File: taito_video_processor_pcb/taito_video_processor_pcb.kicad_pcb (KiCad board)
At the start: 2 copper layers, 304.8 x 279.4 mm, 112 parts, among them U1 245_1, U10 4116, U100 LS00, U101 LS08, U102 LS10, U103 LS00, U104 157_1, U105 299_1, U106 299_1, U107 299_1, U108 299_1, U109 299_1, U11 4116, U110 299_1, U12 4116, U13 4116, U14 4116, U15 4116, U16 4116, U17 4116, U18 68A45, U19 86_2, U2 245_1, U20 86_1, U21 157_1, U22 LS32, U23 161_1, U24 LS04, U25 374_1, U26 4116, U27 4116, U28 4116, U29 4116, U3 2114, U30 4116, U31 4116, U32 4116, U33 4116, U34 LS374, U35 153_1, U36 LS74, U37 LS08, U38 74S113, U39 LS04, U4 2114, U40 7417, U41 4116, U42 4116, U43 4116, U44 4116, U45 4116, U46 4116, U47 4116, U48 4116, U49 LS32, U5 157_1, U50 86_3, U51 LS86, U52 153_1, U53 153_1, U54 153_1, U55 157_1, U56 2148_1, U57 2148_2, U58 7417, U59 4116, U6 157_1, U60 4116, U61 4116, U62 4116, U63 4116, U64 4116, U65 4116, U66 4116, U67 LS32, U68 244_2, U69 245_1, U7 LS74, U70 374_1, U71 374_1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

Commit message: Continued layout
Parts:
- added J3: 50pin, taito_video_processor_pcb:50Pin, F.Cu at (208.3, 342.9)
- added J6: 50pin, taito_video_processor_pcb:50Pin, F.Cu at (208.3, 90.2)
- added REF**: hole_15, taito_video_processor_pcb:hole_15, F.Cu at (355.6, 83.8)
- added REF**: hole_15, taito_video_processor_pcb:hole_15, F.Cu at (449.6, 83.8)
- added REF**: hole_15, taito_video_processor_pcb:hole_15, F.Cu at (161.3, 84.5)
- added REF**: hole_15, taito_video_processor_pcb:hole_15, F.Cu at (160.0, 348.0)
- moved REF** 0.63 mm to (449.6, 348.0)
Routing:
- added copper zone on B.Cu, net GND

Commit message: Placed components
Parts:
- added C1: .1uf, taito_video_processor_pcb:GenericComp, F.Cu at (299.7, 86.4)
- added C10: .1uf, taito_video_processor_pcb:GenericComp, F.Cu at (176.5, 104.1)
- added C11: .1uf, taito_video_processor_pcb:GenericComp, F.Cu at (196.8, 123.8)
- added C12: .1uf, taito_video_processor_pcb:GenericComp, F.Cu at (207.6, 115.6)
- added C13: .1uf, taito_video_processor_pcb:GenericComp, F.Cu at (255.3, 101.6)
- added C14: 100pf, taito_video_processor_pcb:GenericComp, F.Cu at (269.2, 108.0)
- added C15: .1uf, taito_video_processor_pcb:GenericComp, F.Cu at (284.5, 109.2)
- added C16: .1uf, taito_video_processor_pcb:GenericComp, F.Cu at (316.2, 111.8)
- added C17: .1uf, taito_video_processor_pcb:GenericComp, F.Cu at (331.5, 111.8)
- added C18: .1uf, taito_video_processor_pcb:GenericComp, F.Cu at (346.7, 111.8)
- added C19: .1uf, taito_video_processor_pcb:GenericComp, F.Cu at (361.9, 111.8)
- added C2: .1uf, taito_video_processor_pcb:GenericComp, F.Cu at (303.5, 90.2)
- added C20: .1uf, taito_video_processor_pcb:GenericComp, F.Cu at (377.2, 111.8)
- added C21: .1uf, taito_video_processor_pcb:GenericComp, F.Cu at (392.4, 111.8)
- added C22: 10uf, taito_video_processor_pcb:CapA, F.Cu at (406.4, 101.6)
- added C23: .1uf, taito_video_processor_pcb:GenericComp, F.Cu at (420.4, 97.8)
- added C24: .1uf, taito_video_processor_pcb:GenericComp, F.Cu at (448.3, 99.1)
- added C25: .1uf, taito_video_processor_pcb:GenericComp, F.Cu at (448.3, 104.1)
- added C26: .1uf, taito_video_processor_pcb:GenericComp, F.Cu at (161.3, 138.4)
- added C27: .1uf, taito_video_processor_pcb:GenericComp, F.Cu at (189.2, 139.7)
- added C28: .1uf, taito_video_processor_pcb:GenericComp, F.Cu at (207.0, 143.5)
- added C29: .1uf, taito_video_processor_pcb:GenericComp, F.Cu at (224.8, 146.1)
- added C3: .1uf, taito_video_processor_pcb:GenericComp, F.Cu at (318.8, 90.2)
- added C30: .1uf, taito_video_processor_pcb:GenericComp, F.Cu at (237.5, 148.6)
- added C31: 100pf, taito_video_processor_pcb:GenericComp, F.Cu at (271.8, 123.2)
- added C32: .1uf, taito_video_processor_pcb:GenericComp, F.Cu at (285.8, 151.1)
- added C33: .1uf, taito_video_processor_pcb:GenericComp, F.Cu at (312.4, 127.6)
- added C34: .1uf, taito_video_processor_pcb:GenericComp, F.Cu at (329.6, 127.6)
- added C35: .1uf, taito_video_processor_pcb:GenericComp, F.Cu at (316.2, 146.1)
- added C36: .1uf, taito_video_processor_pcb:GenericComp, F.Cu at (331.5, 146.1)
- added C37: .1uf, taito_video_processor_pcb:GenericComp, F.Cu at (346.7, 146.1)
- added C38: .1uf, taito_video_processor_pcb:GenericComp, F.Cu at (360.7, 134.6)
- added C39: .1uf, taito_video_processor_pcb:GenericComp, F.Cu at (361.9, 146.1)
- added C4: .1uf, taito_video_processor_pcb:GenericComp, F.Cu at (334.0, 90.2)
- added C40: .1uf, taito_video_processor_pcb:GenericComp, F.Cu at (375.9, 134.6)
- added C41: .1uf, taito_video_processor_pcb:GenericComp, F.Cu at (377.2, 146.1)
- added C42: 10uf, taito_video_processor_pcb:CapA, F.Cu at (391.8, 135.9)
- added C43: .1uf, taito_video_processor_pcb:GenericComp, F.Cu at (398.8, 127.6)
- added C44: 10uf, taito_video_processor_pcb:CapA, F.Cu at (407.7, 128.9)
- added C45: 10uf, taito_video_processor_pcb:CapA, F.Cu at (417.8, 127.0)
- added C46: .1uf, taito_video_processor_pcb:GenericComp, F.Cu at (448.3, 129.5)
- added C47: .1uf, taito_video_processor_pcb:GenericComp, F.Cu at (448.3, 134.6)
- added C48: .1uf, taito_video_processor_pcb:GenericComp, F.Cu at (448.3, 139.7)
- added C49: .1uf, taito_video_processor_pcb:GenericComp, F.Cu at (448.3, 151.1)
- added C5: .1uf, taito_video_processor_pcb:GenericComp, F.Cu at (349.2, 90.2)
- added C50: .1uf, taito_video_processor_pcb:GenericComp, F.Cu at (222.2, 181.6)
- added C51: .1uf, taito_video_processor_pcb:GenericComp, F.Cu at (255.3, 174.0)
- added C52: .1uf, taito_video_processor_pcb:GenericComp, F.Cu at (270.5, 174.0)
- added C53: .1uf, taito_video_processor_pcb:GenericComp, F.Cu at (307.3, 163.8)
- added C54: .1uf, taito_video_processor_pcb:GenericComp, F.Cu at (321.3, 162.6)
- added C55: .1uf, taito_video_processor_pcb:GenericComp, F.Cu at (314.3, 181.6)
- added C56: .1uf, taito_video_processor_pcb:GenericComp, F.Cu at (331.5, 181.6)
- added C57: .1uf, taito_video_processor_pcb:GenericComp, F.Cu at (336.6, 163.2)
- added C58: .1uf, taito_video_processor_pcb:GenericComp, F.Cu at (351.8, 163.2)
- added C59: .1uf, taito_video_processor_pcb:GenericComp, F.Cu at (361.9, 181.6)
- added C6: .1uf, taito_video_processor_pcb:GenericComp, F.Cu at (364.5, 90.2)
- added C60: .1uf, taito_video_processor_pcb:GenericComp, F.Cu at (377.2, 181.6)
- added C61: 10uf, taito_video_processor_pcb:CapA, F.Cu at (391.8, 171.4)
- added C62: .1uf, taito_video_processor_pcb:GenericComp, F.Cu at (398.8, 163.8)
- added C63: 10uf, taito_video_processor_pcb:CapA, F.Cu at (407.0, 167.6)
- added C64: .1uf, taito_video_processor_pcb:GenericComp, F.Cu at (414.0, 162.6)
- added C65: 470pf, taito_video_processor_pcb:GenericComp, F.Cu at (448.3, 162.6)
- added C66: .1uf, taito_video_processor_pcb:GenericComp, F.Cu at (448.3, 168.9)
- added C67: .1uf, taito_video_processor_pcb:GenericComp, F.Cu at (161.3, 199.4)
- added C68: .1uf, taito_video_processor_pcb:GenericComp, F.Cu at (207.6, 209.6)
- added C69: .1uf, taito_video_processor_pcb:GenericComp, F.Cu at (239.4, 209.6)
- added C7: .1uf, taito_video_processor_pcb:GenericComp, F.Cu at (379.7, 90.2)
- added C70: .1uf, taito_video_processor_pcb:GenericComp, F.Cu at (253.4, 209.6)
- added C71: .1uf, taito_video_processor_pcb:GenericComp, F.Cu at (269.2, 209.6)
- added C72: .1uf, taito_video_processor_pcb:GenericComp, F.Cu at (316.2, 217.2)
- added C73: .1uf, taito_video_processor_pcb:GenericComp, F.Cu at (322.6, 199.4)
- added C74: .1uf, taito_video_processor_pcb:GenericComp, F.Cu at (337.8, 199.4)
- added C75: .1uf, taito_video_processor_pcb:GenericComp, F.Cu at (346.7, 217.2)
- added C76: .1uf, taito_video_processor_pcb:GenericComp, F.Cu at (377.2, 217.2)
- added C77: 10uf, taito_video_processor_pcb:CapA, F.Cu at (391.8, 207.0)
- added C78: .1uf, taito_video_processor_pcb:GenericComp, F.Cu at (398.8, 199.4)
- added C79: .1uf, taito_video_processor_pcb:GenericComp, F.Cu at (406.4, 217.2)
- added C8: .1uf, taito_video_processor_pcb:GenericComp, F.Cu at (395.0, 90.2)
- added C80: 10uf, taito_video_processor_pcb:CapA, F.Cu at (408.3, 197.5)
- added C81: .1uf, taito_video_processor_pcb:GenericComp, F.Cu at (413.4, 191.1)
- added C82: .1uf, taito_video_processor_pcb:GenericComp, F.Cu at (448.3, 204.5)
- added C87: .1uf, taito_video_processor_pcb:GenericComp, F.Cu at (440.1, 226.1)
- added C9: 10uf, taito_video_processor_pcb:CapA, F.Cu at (408.3, 88.9)
- added FB1: Ferrite_Bead, taito_video_processor_pcb:FB, F.Cu at (422.9, 109.2)
- added FB2: Ferrite_Bead, taito_video_processor_pcb:FB, F.Cu at (428.0, 109.2)
- added FB3: Ferrite_Bead, taito_video_processor_pcb:FB, F.Cu at (422.9, 123.8)
- added FB4: Ferrite_Bead, taito_video_processor_pcb:FB, F.Cu at (422.9, 141.0)
- added FB5: Ferrite_Bead, taito_video_processor_pcb:FB, F.Cu at (428.0, 141.0)
- added FB6: Ferrite_Bead, taito_video_processor_pcb:FB, F.Cu at (422.9, 157.5)
- added FB7: Ferrite_Bead, taito_video_processor_pcb:FB, F.Cu at (428.0, 157.5)
- added J1: 14pin, taito_video_processor_pcb:con_14pin, F.Cu at (434.3, 306.4)
- added J19: 2pin, taito_video_processor_pcb:con_2pin, F.Cu at (434.3, 160.0)
- added J2: 14pin, taito_video_processor_pcb:con_14pin, F.Cu at (434.3, 123.5)
- added Q1: 2N3904, taito_video_processor_pcb:Trans, F.Cu at (279.4, 198.1)
- added Q2: 2N3904, taito_video_processor_pcb:Trans, F.Cu at (287.0, 198.1)
- added Q3: 2N3904, taito_video_processor_pcb:Trans, F.Cu at (287.0, 190.5)
- added Q4: 2N3904, taito_video_processor_pcb:Trans, F.Cu at (297.2, 190.5)
- added Q5: 2N3904, taito_video_processor_pcb:Trans, F.Cu at (297.2, 198.1)
- added Q6: 2N3904, taito_video_processor_pcb:Trans, F.Cu at (299.7, 207.0)
- added Q7: 2N3904, taito_video_processor_pcb:Trans, F.Cu at (299.7, 217.2)
- added Q8: 2N3905, taito_video_processor_pcb:Trans, F.Cu at (254.0, 341.6)
- added R1: 33, taito_video_processor_pcb:GenericComp, F.Cu at (420.4, 90.2)
- added R10: 33, taito_video_processor_pcb:GenericComp, F.Cu at (406.4, 143.5)
- added R11: ?, taito_video_processor_pcb:GenericComp, F.Cu at (252.7, 188.0)
- added R12: ?, taito_video_processor_pcb:GenericComp, F.Cu at (268.0, 185.4)
- added R13: 82, taito_video_processor_pcb:GenericComp, F.Cu at (283.2, 179.1)
- added R14: 180, taito_video_processor_pcb:GenericComp, F.Cu at (285.8, 179.1)
- added R15: 270, taito_video_processor_pcb:GenericComp, F.Cu at (283.2, 166.4)
- added R16: 150, taito_video_processor_pcb:GenericComp, F.Cu at (285.8, 166.4)
- added R17: 150, taito_video_processor_pcb:GenericComp, F.Cu at (298.4, 166.4)
- added R18: 270, taito_video_processor_pcb:GenericComp, F.Cu at (301.0, 166.4)
- added R19: 180, taito_video_processor_pcb:GenericComp, F.Cu at (298.4, 179.1)
- added R2: 1.5k, taito_video_processor_pcb:GenericComp, F.Cu at (274.3, 123.2)
- added R20: 82, taito_video_processor_pcb:GenericComp, F.Cu at (301.0, 179.1)
- added R21: 33, taito_video_processor_pcb:GenericComp, F.Cu at (422.9, 180.3)
- added R22: ?, taito_video_processor_pcb:GenericComp, F.Cu at (203.2, 199.4)
- added R23: ?, taito_video_processor_pcb:GenericComp, F.Cu at (208.3, 195.6)
- added R24: ?, taito_video_processor_pcb:GenericComp, F.Cu at (218.4, 191.8)
- added R25: ?, taito_video_processor_pcb:GenericComp, F.Cu at (223.5, 205.7)
- added R26: ?, taito_video_processor_pcb:GenericComp, F.Cu at (269.2, 196.8)
- added R27: ?, taito_video_processor_pcb:GenericComp, F.Cu at (269.2, 199.4)
- added R28: 180, taito_video_processor_pcb:GenericComp, F.Cu at (283.2, 195.6)
- added R29: 470, taito_video_processor_pcb:GenericComp, F.Cu at (290.8, 195.6)
- added R3: 270, taito_video_processor_pcb:GenericComp, F.Cu at (284.5, 119.4)
- added R30: 470, taito_video_processor_pcb:GenericComp, F.Cu at (293.4, 195.6)
- added R31: 470, taito_video_processor_pcb:GenericComp, F.Cu at (301.0, 195.6)
- added R32: 470, taito_video_processor_pcb:GenericComp, F.Cu at (303.5, 195.6)
- added R33: 470, taito_video_processor_pcb:GenericComp, F.Cu at (306.1, 195.6)
- added R34: 680, taito_video_processor_pcb:GenericComp, F.Cu at (283.2, 209.6)
- added R35: 390, taito_video_processor_pcb:GenericComp, F.Cu at (285.8, 209.6)
- added R36: 33, taito_video_processor_pcb:GenericComp, F.Cu at (422.9, 212.1)
- added R39: 330, taito_video_processor_pcb:GenericComp, F.Cu at (225.4, 231.1)
- added R4: 270, taito_video_processor_pcb:GenericComp, F.Cu at (284.5, 121.9)
- added R40: 330, taito_video_processor_pcb:GenericComp, F.Cu at (230.5, 231.1)
- added R41: 330, taito_video_processor_pcb:GenericComp, F.Cu at (233.0, 231.1)
- added R42: 330, taito_video_processor_pcb:GenericComp, F.Cu at (235.6, 231.1)
- added R43: 330, taito_video_processor_pcb:GenericComp, F.Cu at (238.1, 231.1)
- added R44: 330, taito_video_processor_pcb:GenericComp, F.Cu at (240.7, 231.1)
- added R5: 270, taito_video_processor_pcb:GenericComp, F.Cu at (284.5, 124.5)
- added R6: 3.3k, taito_video_processor_pcb:GenericComp, F.Cu at (255.3, 138.4)
- added R7: 220, taito_video_processor_pcb:GenericComp, F.Cu at (268.0, 141.0)
- added R8: 2.2k, taito_video_processor_pcb:GenericComp, F.Cu at (270.5, 141.0)
- added R9: ?, taito_video_processor_pcb:GenericComp, F.Cu at (299.7, 130.8)
- added RP1: 1K, taito_video_processor_pcb:RP, F.Cu at (299.7, 108.0)
- added RP2: 47K, taito_video_processor_pcb:RP, F.Cu at (161.9, 299.7)
- added RP3: 3.3k, taito_video_processor_pcb:RP, F.Cu at (193.7, 287.0)
- added RP4: 3.3k, taito_video_processor_pcb:RP, F.Cu at (193.7, 322.6)
- added RP5: 3.3k, taito_video_processor_pcb:RP, F.Cu at (234.9, 334.0)
- added TP1: TestPoint, taito_video_processor_pcb:TPA, F.Cu at (278.1, 94.6)
- added TP2: 10MHz, taito_video_processor_pcb:TPA, F.Cu at (257.8, 158.8)
- added TP3: TestPoint, taito_video_processor_pcb:TPA, F.Cu at (240.0, 195.6)
- added TP4: TestPoint, taito_video_processor_pcb:TPA, F.Cu at (242.6, 196.2)
- added Y1: Crystal, taito_video_processor_pcb:Crystal, F.Cu at (265.4, 120.7)
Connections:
- net MUX renamed Net-(U36-Pad11)
- U35 pad 7: M4 -> Net-(R24-Pad2)
- U35 pad 9: M3 -> Net-(R11-Pad2)
- U37 pad 8: ~RAS -> Net-(R12-Pad2)
- U52 pad 7: M6 -> Net-(R22-Pad2)
- U52 pad 9: M5 -> Net-(R23-Pad2)
- U53 pad 7: M2 -> Net-(R26-Pad2)
- U53 pad 9: M1 -> Net-(R27-Pad2)
- U54 pad 7: M0 -> Net-(R25-Pad2)
- U67 pad 2: ~EVEN1 -> ~ODD1
- U67 pad 5: ~ODD1 -> ~EVEN1
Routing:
- net GND: track 0.00 -> 37.6 mm, vias 0 -> 4
- net +5V: track 0.00 -> 10.2 mm
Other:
- board text added: "1"
- board text added: "1 2"
- board text added: "C 10"
- board text added: "C 12"
- board text added: "C 14"
- board text added: "C 15"
- board text added: "C 16"
- board text added: "C 17"
- board text added: "C 18"
- board text added: "C 19"
- board text added: "C 20"
- board text added: "C 21"
- board text added: "C 22"
- board text added: "C 27"
- board text added: "C 28"
- board text added: "C 29"
- board text added: "C 30"
- board text added: "C 31"
- board text added: "C 32"
- board text added: "C 35"
- board text added: "C 36"
- board text added: "C 37"
- board text added: "C 38"
- board text added: "C 39"
- board text added: "C 40"
- board text added: "C 41"
- board text added: "C 42"
- board text added: "C 44"
- board text added: "C 45"
- board text added: "C 50"
- board text added: "C 51"
- board text added: "C 52"
- board text added: "C 53"
- board text added: "C 55"
- board text added: "C 56"
- board text added: "C 59"
- board text added: "C 60"
- board text added: "C 61"
- board text added: "C 63"
- board text added: "C 69"
- board text added: "C 76"
- board text added: "C 77"
- board text added: "C 79"
- board text added: "F B 1"
- board text added: "FB 2"
- board text added: "FB 3"
- board text added: "FB 4"
- board text added: "FB 5"
- board text added: "FB 6"
- board text added: "FB 7"
- board text added: "Q 1"
- board text added: "R 11"
- board text added: "R 12"
- board text added: "R 14"
- board text added: "R 15"
- board text added: "R 17"
- board text added: "R 18"
- board text added: "R 2"
- board text added: "R 20"
- board text added: "R 21"
- board text added: "R 25"
- board text added: "R 36"
- board text added: "R 39"
- board text added: "R 7"
- board text added: "R 8"
- board text added: "RP 2"
- board text added: "RP 3"
- board text added: "U 57"
- board text added: "U 59"
- board text added: "U 60"
- board text added: "U 61"

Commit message: Finished placing components
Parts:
- added BT1: 3.6V, taito_video_processor_pcb:battery, F.Cu at (292.7, 344.2)
- added C100: .1uf, taito_video_processor_pcb:GenericComp, F.Cu at (246.4, 330.2)
- added C101: 10uf, taito_video_processor_pcb:GenericComp, F.Cu at (259.1, 330.2)
- added C102: .1uf, taito_video_processor_pcb:GenericComp, F.Cu at (283.8, 321.3)
- added C103: .1uf, taito_video_processor_pcb:GenericComp, F.Cu at (313.7, 308.6)
- added C104: .1uf, taito_video_processor_pcb:GenericComp, F.Cu at (330.2, 316.2)
- added C105: .1uf, taito_video_processor_pcb:GenericComp, F.Cu at (344.8, 316.2)
- added C106: .1uf, taito_video_processor_pcb:GenericComp, F.Cu at (377.2, 316.2)
- added C107: .1uf, taito_video_processor_pcb:GenericComp, F.Cu at (389.9, 316.2)
- added C108: .1uf, taito_video_processor_pcb:GenericComp, F.Cu at (412.8, 316.9)
- added C109: 100uf, taito_video_processor_pcb:CapB, F.Cu at (411.5, 338.5)
- added C110: 470pf, taito_video_processor_pcb:GenericComp, F.Cu at (447.0, 306.7)
- added C111: 470pf, taito_video_processor_pcb:GenericComp, F.Cu at (447.0, 322.6)
- added C112: 470pf, taito_video_processor_pcb:GenericComp, F.Cu at (447.0, 326.4)
- added C113: 470pf, taito_video_processor_pcb:GenericComp, F.Cu at (447.0, 330.2)
- added C83: .1uf, taito_video_processor_pcb:GenericComp, F.Cu at (161.3, 237.5)
- added C84: .1uf, taito_video_processor_pcb:GenericComp, F.Cu at (260.4, 262.9)
- added C85: .1uf, taito_video_processor_pcb:GenericComp, F.Cu at (304.2, 251.5)
- added C86: .1uf, taito_video_processor_pcb:GenericComp, F.Cu at (381.0, 243.2)
- added C88: 100uf, taito_video_processor_pcb:CapB, F.Cu at (425.4, 255.9)
- added C89: 100uf, taito_video_processor_pcb:CapB, F.Cu at (434.3, 255.9)
- added C90: 100uf, taito_video_processor_pcb:CapB, F.Cu at (443.2, 247.0)
- added C91: .1uf, taito_video_processor_pcb:GenericComp, F.Cu at (448.3, 231.8)
- added C92: .1uf, taito_video_processor_pcb:GenericComp, F.Cu at (161.9, 278.8)
- added C93: .1uf, taito_video_processor_pcb:GenericComp, F.Cu at (283.2, 285.8)
- added C94: .1uf, taito_video_processor_pcb:GenericComp, F.Cu at (314.3, 280.7)
- added C95: .1uf, taito_video_processor_pcb:GenericComp, F.Cu at (416.6, 278.8)
- added C96: 470pf, taito_video_processor_pcb:GenericComp, F.Cu at (448.3, 278.8)
- added C97: 470pf, taito_video_processor_pcb:GenericComp, F.Cu at (447.0, 290.8)
- added C98: 470pf, taito_video_processor_pcb:GenericComp, F.Cu at (447.0, 298.4)
- added C99: .1uf, taito_video_processor_pcb:GenericComp, F.Cu at (240.0, 316.2)
- added FB10: Ferrite_Bead, taito_video_processor_pcb:FB, F.Cu at (422.9, 298.4)
- added FB11: Ferrite_Bead, taito_video_processor_pcb:FB, F.Cu at (422.9, 306.7)
- added FB12: Ferrite_Bead, taito_video_processor_pcb:FB, F.Cu at (422.9, 321.9)
- added FB13: Ferrite_Bead, taito_video_processor_pcb:FB, F.Cu at (422.9, 326.4)
- added FB14: Ferrite_Bead, taito_video_processor_pcb:FB, F.Cu at (442.0, 340.4)
- added FB8: Ferrite_Bead, taito_video_processor_pcb:FB, F.Cu at (443.2, 271.1)
- added FB9: Ferrite_Bead, taito_video_processor_pcb:FB, F.Cu at (422.9, 290.8)
- added JB2: W1, taito_video_processor_pcb:JMP, F.Cu at (326.4, 345.4)
- added LED1: LED, taito_video_processor_pcb:LED, F.Cu at (172.7, 229.9)
- added LED2: LED, taito_video_processor_pcb:LED, F.Cu at (181.6, 229.9)
- added LED3: LED, taito_video_processor_pcb:LED, F.Cu at (196.8, 229.9)
- added LED4: LED, taito_video_processor_pcb:LED, F.Cu at (204.5, 229.9)
- added LED5: LED, taito_video_processor_pcb:LED, F.Cu at (212.1, 229.9)
- added LED6: LED, taito_video_processor_pcb:LED, F.Cu at (218.4, 229.9)
- added R37: 47k, taito_video_processor_pcb:GenericComp, F.Cu at (167.6, 229.9)
- added R38: 3.3k, taito_video_processor_pcb:GenericComp, F.Cu at (186.7, 234.9)
- added R45: 150, taito_video_processor_pcb:GenericComp, F.Cu at (288.3, 231.1)
- added R46: 82, taito_video_processor_pcb:GenericComp, F.Cu at (297.8, 231.1)
- added R47: 470, taito_video_processor_pcb:GenericComp, F.Cu at (300.4, 231.1)
- added R48: 180, taito_video_processor_pcb:GenericComp, F.Cu at (302.9, 231.1)
- added R49: 270, taito_video_processor_pcb:GenericComp, F.Cu at (308.0, 231.1)
- added R50: 47k, taito_video_processor_pcb:GenericComp, F.Cu at (177.8, 240.0)
- added R51: 33, taito_video_processor_pcb:GenericComp, F.Cu at (309.2, 245.1)
- added R52: 33, taito_video_processor_pcb:GenericComp, F.Cu at (312.4, 245.1)
- added R53: 33, taito_video_processor_pcb:GenericComp, F.Cu at (330.8, 246.4)
- added R54: 33, taito_video_processor_pcb:GenericComp, F.Cu at (346.1, 241.3)
- added R55: 33, taito_video_processor_pcb:GenericComp, F.Cu at (361.3, 241.3)
- added R56: 33, taito_video_processor_pcb:GenericComp, F.Cu at (378.5, 248.9)
- added R57: 33, taito_video_processor_pcb:GenericComp, F.Cu at (392.4, 245.1)
- added R58: 33, taito_video_processor_pcb:GenericComp, F.Cu at (401.3, 245.1)
- added R59: 47k, taito_video_processor_pcb:GenericComp, F.Cu at (161.9, 264.2)
- added R60: 3.3k, taito_video_processor_pcb:GenericComp, F.Cu at (190.5, 271.1)
- added R61: 390, taito_video_processor_pcb:GenericComp, F.Cu at (254.0, 287.0)
- added R62: 3.3k, taito_video_processor_pcb:GenericComp, F.Cu at (285.1, 280.7)
- added R63: 1k, taito_video_processor_pcb:GenericComp, F.Cu at (188.6, 321.3)
- added R64: 120, taito_video_processor_pcb:GenericComp, F.Cu at (259.1, 333.4)
- added R65: 150, taito_video_processor_pcb:GenericComp, F.Cu at (259.1, 336.6)
- added R66: 3.3k, taito_video_processor_pcb:GenericComp, F.Cu at (284.5, 307.3)
- added R67: 3.3k, taito_video_processor_pcb:GenericComp, F.Cu at (309.9, 302.3)
- added R68: 3.3k, taito_video_processor_pcb:GenericComp, F.Cu at (375.3, 307.3)
- added R69: 3.3k, taito_video_processor_pcb:GenericComp, F.Cu at (393.7, 307.3)
- added REF**: hole, taito_video_processor_pcb:hole, F.Cu at (176.5, 271.1)
- added REF**: hole, taito_video_processor_pcb:hole, F.Cu at (176.5, 328.3)
- added REF**: hole, taito_video_processor_pcb:hole, F.Cu at (292.7, 335.9)
- added REF**: hole, taito_video_processor_pcb:hole, F.Cu at (292.7, 352.4)
- added SW1: SW_Push, taito_video_processor_pcb:Switch, F.Cu at (168.9, 332.7)
- added TP5: TestPoint, taito_video_processor_pcb:TPB, F.Cu at (163.2, 243.8)
- added TP6: TestPoint, taito_video_processor_pcb:TPB, F.Cu at (194.3, 302.3)
- added TP7: TestPoint, taito_video_processor_pcb:TPB, F.Cu at (307.3, 297.8)
- added TP8: TestPoint, taito_video_processor_pcb:TPB, F.Cu at (224.8, 336.6)
- moved J1 3.89 mm to (434.3, 302.5), turned to 270 degrees
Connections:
- J1 pad 12: Net-(J1-Pad12) -> SPARE2
- J1 pad 13: Net-(J1-Pad13) -> SPARE3
- J1 pad 8: Net-(J1-Pad8) -> SPARE1
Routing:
- net GND: track 37.6 -> 113.2 mm
- net _+5V_: track 0.00 -> 15.4 mm
- net SPARE2: track 0.00 -> 14.6 mm
- net SPARE1: track 0.00 -> 14.1 mm
- net _-5V_: track 0.00 -> 14.1 mm
- net _+12V_: track 0.00 -> 14.1 mm
- net SPARE3: track 0.00 -> 14.0 mm
- net _MRST_: track 0.00 -> 12.7 mm
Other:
- board text added: "2"
- board text added: "3"
- board text added: "4"
- board text added: "5"
- board text added: "6"
- board text added: "BATTERY"
- board text added: "C 100"
- board text added: "C 103"
- board text added: "C 104"
- board text added: "C 106"
- board text added: "C 107"
- board text added: "C 112"
- board text added: "C 84"
- board text added: "C 85"
- board text added: "C 86"
- board text added: "C 89"
- board text added: "C 92"
- board text added: "C 93"
- board text added: "C 99"
- board text added: "LED"
- board text added: "R 38"
- board text added: "R 46"
- board text added: "R 47"
- board text added: "R 52"
- board text added: "R 53"
- board text added: "R 54"
- board text added: "R 55"
- board text added: "R 56"
- board text added: "R 61"
- board text added: "R 62"
- board text added: "R 63"
- board text added: "TP 8"
- board text added: "U 104"
- board text added: "U 107"
- board text added: "U 108"
- board text added: "U 109"
- board text added: "U 110"

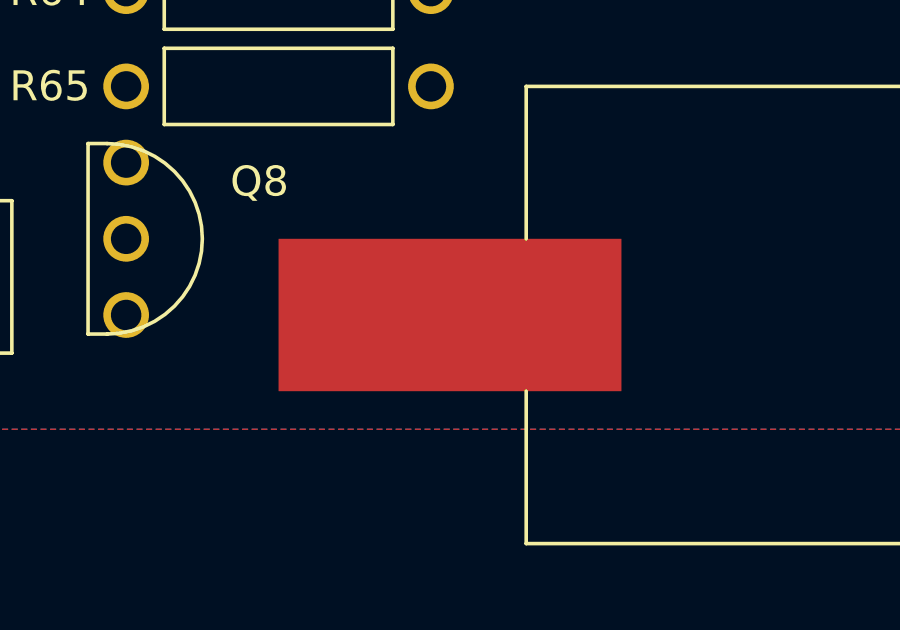
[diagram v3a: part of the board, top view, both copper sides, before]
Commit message: Finished placing components
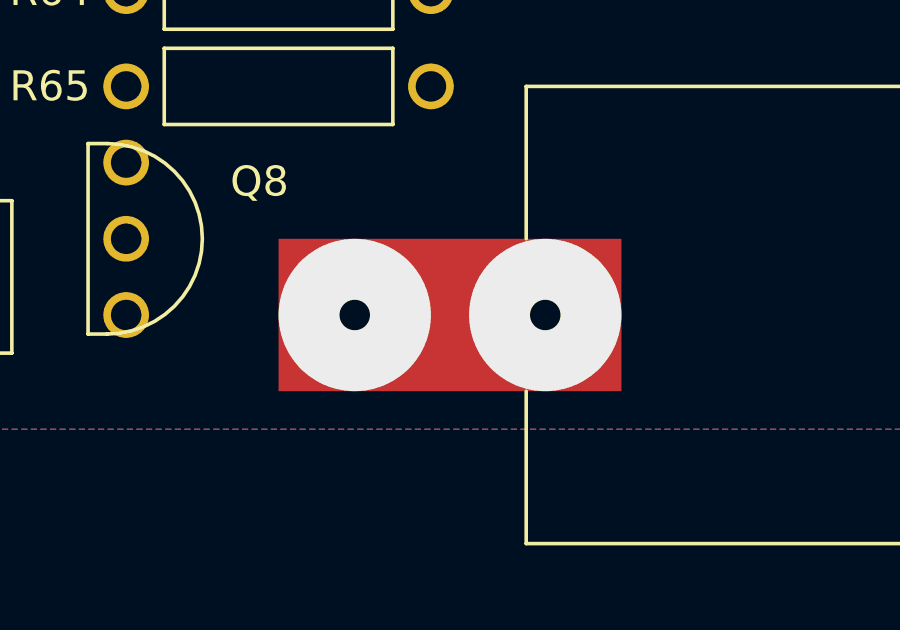
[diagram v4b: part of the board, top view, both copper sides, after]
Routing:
- net Net-(BT1-Pad1): vias 0 -> 2
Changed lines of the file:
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@@
     (thickness 1.6)
     (drawings 116)
-    (tracks 42)
+    (tracks 44)
     (zones 0)
     (modules 352)
@@
   (gr_line (start 152.4 355.6) (end 152.4 76.2) (layer Edge.Cuts) (width 0.0254))
   (gr_line (start 152.4 355.6) (end 457.2 355.6) (layer Edge.Cuts) (width 0.0254))
+  (via (at 267.97 344.17) (size 5.08) (drill 1.016) (layers F.Cu B.Cu) (net 545))
+  (via (at 261.62 344.17) (size 5.08) (drill 1.016) (layers F.Cu B.Cu) (net 545))
   (segment (start 443.23 168.91) (end 433.07 168.91) (width 1.016) (layer F.Cu) (net 1))
   (via (at 224.79 81.28) (size 1.524) (drill 1.016) (layers F.Cu B.Cu) (net 18))

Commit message: Added ground vias
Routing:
- net GND: vias 4 -> 17
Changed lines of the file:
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@@
     (thickness 1.6)
     (drawings 116)
-    (tracks 44)
+    (tracks 57)
     (zones 0)
     (modules 352)
@@
   (segment (start 434.34 318.389) (end 452.374 318.389) (width 1.016) (layer F.Cu) (net 18))
   (segment (start 452.374 318.389) (end 452.755 318.77) (width 1.016) (layer F.Cu) (net 18))
+  (via (at 156.21 107.95) (size 1.524) (drill 1.016) (layers F.Cu B.Cu) (net 18))
+  (via (at 156.21 168.91) (size 1.524) (drill 1.016) (layers F.Cu B.Cu) (net 18))
+  (via (at 156.21 290.83) (size 1.524) (drill 1.016) (layers F.Cu B.Cu) (net 18))
+  (via (at 156.21 317.5) (size 1.524) (drill 1.016) (layers F.Cu B.Cu) (net 18))
+  (via (at 167.64 351.79) (size 1.524) (drill 1.016) (layers F.Cu B.Cu) (net 18))
+  (via (at 194.31 351.79) (size 1.524) (drill 1.016) (layers F.Cu B.Cu) (net 18))
+  (via (at 220.98 351.79) (size 1.524) (drill 1.016) (layers F.Cu B.Cu) (net 18))
+  (via (at 246.38 351.79) (size 1.524) (drill 1.016) (layers F.Cu B.Cu) (net 18))
+  (via (at 315.595 351.79) (size 1.524) (drill 1.016) (layers F.Cu B.Cu) (net 18))
+  (via (at 344.17 351.79) (size 1.524) (drill 1.016) (layers F.Cu B.Cu) (net 18))
+  (via (at 370.84 351.79) (size 1.524) (drill 1.016) (layers F.Cu B.Cu) (net 18))
+  (via (at 396.24 351.79) (size 1.524) (drill 1.016) (layers F.Cu B.Cu) (net 18))
+  (via (at 423.545 351.79) (size 1.524) (drill 1.016) (layers F.Cu B.Cu) (net 18))
   (segment (start 434.213 298.45) (end 434.34 298.577) (width 1.016) (layer F.Cu) (net 485))
   (segment (start 427.99 298.45) (end 434.213 298.45) (width 1.016) (layer F.Cu) (net 485))

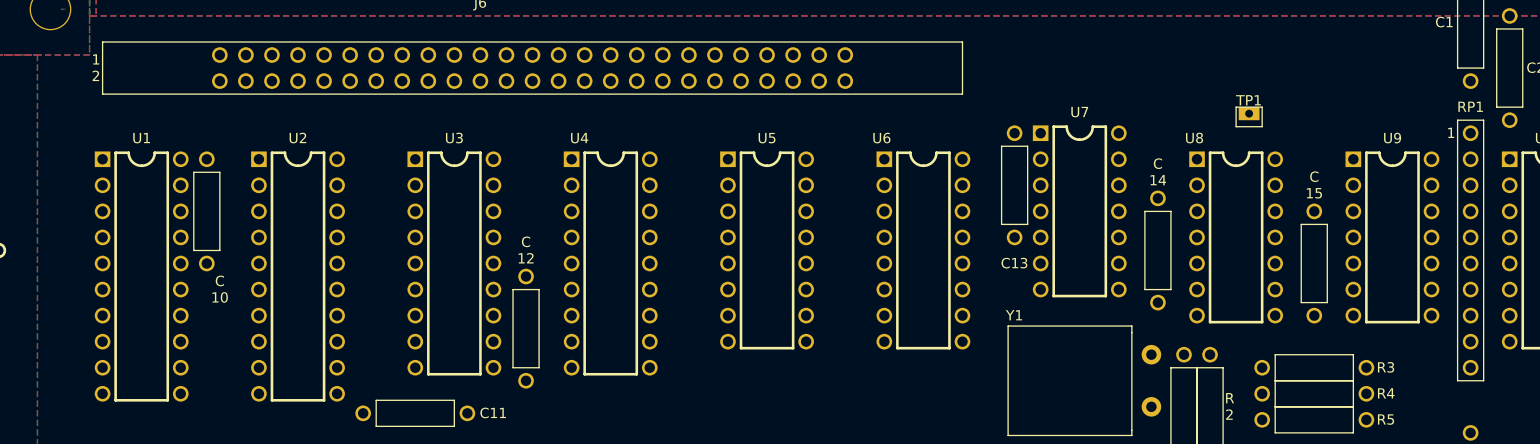
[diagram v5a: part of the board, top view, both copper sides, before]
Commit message: Began laying down traces to figure out the best spacing and via sizes
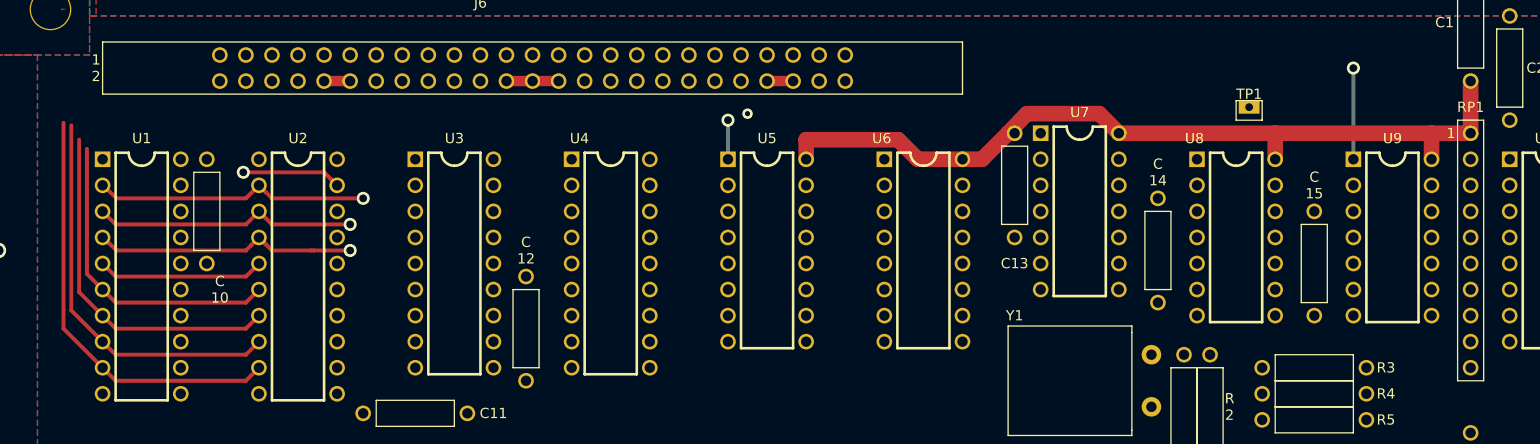
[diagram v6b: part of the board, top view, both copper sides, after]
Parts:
- moved TP1 0.63 mm to (278.1, 94.0)
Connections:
- SW1 pad : (no net) -> GND
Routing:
- net +5V: track 10.2 -> 91.1 mm
- net Net-(U1-Pad9): track 0.00 -> 41.7 mm
- net Net-(U1-Pad8): track 0.00 -> 38.6 mm
- net Net-(U1-Pad7): track 0.00 -> 34.4 mm
- net Net-(U1-Pad6): track 0.00 -> 30.6 mm
- net Net-(U1-Pad2): track 0.00 -> 26.9 mm, vias 0 -> 1
- net Net-(U1-Pad3): track 0.00 -> 25.7 mm, vias 0 -> 1
- net Net-(U1-Pad4): track 0.00 -> 25.7 mm, vias 0 -> 1
- net Net-(U1-Pad5): track 0.00 -> 16.3 mm
- net GND: track 113.2 -> 123.4 mm
- net DPMUX: track 0.00 -> 9.67 mm, vias 0 -> 1
- net ~DS3: track 0.00 -> 8.89 mm, vias 0 -> 1
- net ~DPMUX: track 0.00 -> 3.81 mm, vias 0 -> 1
- net INV: vias 0 -> 1

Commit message: Added traces
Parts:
- moved C14 0.51 mm to (269.2, 108.5)
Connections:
- C2 pad 1: +5V -> -5V
- C3 pad 1: +5V -> -5V
- C4 pad 1: +5V -> -5V
- C5 pad 1: +5V -> -5V
- C6 pad 1: +5V -> -5V
- C7 pad 1: +5V -> -5V
- C8 pad 1: +5V -> -5V
- SW1 pad : GND -> (no net)
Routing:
- net +5V: track 91.1 -> 370.0 mm
- net -5V: track 0.00 -> 224.0 mm
- net GND: track 123.4 -> 341.4 mm, vias 17 -> 18
- net +12V: track 0.00 -> 140.0 mm, vias 0 -> 7
- net D7: track 0.00 -> 77.4 mm
- net VD7: track 0.00 -> 73.7 mm
- net D6: track 0.00 -> 71.8 mm
- net VD6: track 0.00 -> 68.1 mm
- net D5: track 0.00 -> 66.2 mm
- net Net-(U3-Pad4): track 0.00 -> 65.7 mm
- net VD5: track 0.00 -> 62.5 mm
- net Net-(U1-Pad9): track 41.7 -> 102.4 mm, vias 0 -> 1
- net Net-(R50-Pad2): track 0.00 -> 60.6 mm
- net VD4: track 0.00 -> 56.9 mm
- net Net-(U1-Pad8): track 38.6 -> 94.6 mm, vias 0 -> 1
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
